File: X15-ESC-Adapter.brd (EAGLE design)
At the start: 101.6 x 41.1 mm, 10 parts, among them J1 IPBT-103-H1-T-S, J2 IPBT-103-H1-T-S, J3 IPBT-103-H1-T-S, J4 IPBT-103-H1-T-S

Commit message: Parts Replaced with New Versions
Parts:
- BACKPLANE_CONNECTIONS: value BACKPLANE_ESC_ADAPTER_PWRBKP -> IPS1-112-01-L-DBKP; device X15-ESC-Adapter:BACKPLANE_ESC_ADAPTER_BKP_PWR -> X15-ESC-Adapter:IPS1-BACKPLANE-PWR
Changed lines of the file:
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@@
 </autorouter>
 <elements>
-<element name="BACKPLANE_CONNECTIONS" library="X15-ESC-Adapter" package="BACKPLANE_ESC_ADAPTER_BKP_PWR" value="BACKPLANE_ESC_ADAPTER_PWRBKP" x="0" y="0" smashed="yes">
+<element name="BACKPLANE_CONNECTIONS" library="X15-ESC-Adapter" library_urn="urn:adsk.eagle:library:38003364" package="IPS1-BACKPLANE-PWR" package3d_urn="urn:adsk.eagle:package:37886186/4" value="IPS1-112-01-L-DBKP" x="0" y="0" smashed="yes">
 <attribute name="NAME" x="36.83" y="32.639" size="1.27" layer="25"/>
 </element>
-<element name="H1" library="X15-ESC-Adapter" package="6-32-HOLE" package3d_urn="urn:adsk.eagle:package:24384748/2" value="6-32-HOLE" x="3.302" y="37.8968" smashed="yes">
+<element name="H1" library="X15-ESC-Adapter" package="6-32-HOLE" package3d_urn="urn:adsk.eagle:package:37886189/1" value="6-32-HOLE" x="3.302" y="37.8968" smashed="yes">
 <attribute name="NAME" x="3.302" y="40.1828" size="0.6096" layer="25" font="vector" ratio="20" align="bottom-center"/>
 </element>
-<element name="H2" library="X15-ESC-Adapter" package="6-32-HOLE" package3d_urn="urn:adsk.eagle:package:24384748/2" value="6-32-HOLE" x="98.298" y="37.846" smashed="yes">
+<element name="H2" library="X15-ESC-Adapter" package="6-32-HOLE" package3d_urn="urn:adsk.eagle:package:37886189/1" value="6-32-HOLE" x="98.298" y="37.846" smashed="yes">
 <attribute name="NAME" x="98.298" y="40.132" size="0.6096" layer="25" font="vector" ratio="20" align="bottom-center"/>
 <attribute name="VALUE" x="98.298" y="35.56" size="0.6096" layer="27" font="vector" ratio="20" align="top-center"/>
 </element>
-<element name="H3" library="X15-ESC-Adapter" package="6-32-HOLE" package3d_urn="urn:adsk.eagle:package:24384748/2" value="6-32-HOLE" x="3.302" y="17.272" smashed="yes">
+<element name="H3" library="X15-ESC-Adapter" package="6-32-HOLE" package3d_urn="urn:adsk.eagle:package:37886189/1" value="6-32-HOLE" x="3.302" y="17.272" smashed="yes">
 <attribute name="NAME" x="3.302" y="19.558" size="0.6096" layer="25" font="vector" ratio="20" align="bottom-center"/>
 <attribute name="VALUE" x="3.302" y="14.986" size="0.6096" layer="27" font="vector" ratio="20" align="top-center"/>
 </element>
-<element name="H4" library="X15-ESC-Adapter" package="6-32-HOLE" package3d_urn="urn:adsk.eagle:package:24384748/2" value="6-32-HOLE" x="98.298" y="17.272" smashed="yes">
+<element name="H4" library="X15-ESC-Adapter" package="6-32-HOLE" package3d_urn="urn:adsk.eagle:package:37886189/1" value="6-32-HOLE" x="98.298" y="17.272" smashed="yes">
 <attribute name="NAME" x="98.298" y="19.558" size="0.6096" layer="25" font="vector" ratio="20" align="bottom-center"/>
 <attribute name="VALUE" x="98.298" y="14.986" size="0.6096" layer="27" font="vector" ratio="20" align="top-center"/>
 </element>
-<element name="J1" library="X15-ESC-Adapter" package="IPBT-103-H1-T-S" value="IPBT-103-H1-T-S" x="13.9192" y="27.6098" smashed="yes" rot="R90"/>
-<element name="J2" library="X15-ESC-Adapter" package="IPBT-103-H1-T-S" value="IPBT-103-H1-T-S" x="13.97" y="6.985" smashed="yes" rot="R90"/>
-<element name="J3" library="X15-ESC-Adapter" package="IPBT-103-H1-T-S" value="IPBT-103-H1-T-S" x="87.63" y="27.6352" smashed="yes" rot="R270"/>
-<element name="J4" library="X15-ESC-Adapter" package="IPBT-103-H1-T-S" value="IPBT-103-H1-T-S" x="87.6554" y="6.985" smashed="yes" rot="R270"/>
-<element name="LUMENIER_ESC" library="X15-ESC-Adapter" package="LUMENIER" package3d_urn="urn:adsk.eagle:package:24294694/3" value="LUMENIER" x="27.813" y="0.508" smashed="yes"/>
+<element name="J1" library="X15-ESC-Adapter" package="IPBT-103-H1-T-S" package3d_urn="urn:adsk.eagle:package:37886187/2" value="IPBT-103-H1-T-S" x="13.9192" y="27.6098" smashed="yes" rot="R90"/>
+<element name="J2" library="X15-ESC-Adapter" package="IPBT-103-H1-T-S" package3d_urn="urn:adsk.eagle:package:37886187/2" value="IPBT-103-H1-T-S" x="13.97" y="6.985" smashed="yes" rot="R90"/>
+<element name="J3" library="X15-ESC-Adapter" package="IPBT-103-H1-T-S" package3d_urn="urn:adsk.eagle:package:37886187/2" value="IPBT-103-H1-T-S" x="87.63" y="27.6352" smashed="yes" rot="R270"/>
+<element name="J4" library="X15-ESC-Adapter" package="IPBT-103-H1-T-S" package3d_urn="urn:adsk.eagle:package:37886187/2" value="IPBT-103-H1-T-S" x="87.6554" y="6.985" smashed="yes" rot="R270"/>
+<element name="LUMENIER_ESC" library="X15-ESC-Adapter" package="LUMENIER" package3d_urn="urn:adsk.eagle:package:37886188/1" value="LUMENIER" x="27.813" y="0.508" smashed="yes"/>
 </elements>
 <signals>
@@
 <via x="56.1086" y="28.448" extent="1-16" drill="0.35"/>
 <via x="53.1622" y="28.3718" extent="1-16" drill="0.35"/>
+<wire x1="65.024" y1="36.322" x2="65.024" y2="38.862" width="0" layer="19" extent="1-1"/>
+<wire x1="62.484" y1="38.862" x2="65.024" y2="38.862" width="0" layer="19" extent="1-1"/>
+<wire x1="62.484" y1="36.322" x2="65.024" y2="36.322" width="0" layer="19" extent="1-1"/>
+<wire x1="59.944" y1="38.862" x2="62.484" y2="38.862" width="0" layer="19" extent="1-1"/>
+<wire x1="59.944" y1="36.322" x2="62.484" y2="36.322" width="0" layer="19" extent="1-1"/>
+<wire x1="57.404" y1="38.862" x2="59.944" y2="38.862" width="0" layer="19" extent="1-1"/>
+<wire x1="57.404" y1="36.322" x2="59.944" y2="36.322" width="0" layer="19" extent="1-1"/>
+<wire x1="56.4642" y1="34.036" x2="57.404" y2="36.322" width="0" layer="19" extent="1-1"/>
+<wire x1="56.9722" y1="33.0962" x2="56.4642" y2="34.036" width="0" layer="19" extent="1-1"/>
+<wire x1="54.864" y1="38.862" x2="57.404" y2="38.862" width="0" layer="19" extent="1-1"/>
+<wire x1="54.864" y1="36.322" x2="57.404" y2="36.322" width="0" layer="19" extent="1-1"/>
+<wire x1="52.324" y1="38.862" x2="54.864" y2="38.862" width="0" layer="19" extent="1-1"/>
+<wire x1="52.324" y1="36.322" x2="54.864" y2="36.322" width="0" layer="19" extent="1-1"/>
+<wire x1="52.197" y1="34.2392" x2="52.324" y2="36.322" width="0" layer="19" extent="1-1"/>
+<wire x1="53.8226" y1="32.9946" x2="52.197" y2="34.2392" width="0" layer="19" extent="1-1"/>
+<wire x1="55.303" y1="30.878" x2="53.8226" y2="32.9946" width="0" layer="19" extent="1-1"/>
+<wire x1="56.1086" y1="28.448" x2="55.303" y2="30.878" width="0" layer="19" extent="1-1"/>
+<wire x1="53.1622" y1="28.3718" x2="56.1086" y2="28.448" width="0" layer="19" extent="1-1"/>
+<wire x1="59.0296" y1="29.21" x2="56.1086" y2="28.448" width="0" layer="19" extent="1-1"/>
+<wire x1="58.9534" y1="27.432" x2="59.0296" y2="29.21" width="0" layer="19" extent="1-1"/>
 </signal>
 <signal name="GND">
@@
 <via x="46.3042" y="33.274" extent="1-16" drill="0.35"/>
 <via x="48.641" y="33.782" extent="1-16" drill="0.35"/>
+<wire x1="49.784" y1="36.322" x2="49.784" y2="38.862" width="0" layer="19" extent="1-1"/>
+<wire x1="47.244" y1="38.862" x2="49.784" y2="38.862" width="0" layer="19" extent="1-1"/>
+<wire x1="47.244" y1="36.322" x2="49.784" y2="36.322" width="0" layer="19" extent="1-1"/>
+<wire x1="44.704" y1="38.862" x2="47.244" y2="38.862" width="0" layer="19" extent="1-1"/>
+<wire x1="44.704" y1="36.322" x2="47.244" y2="36.322" width="0" layer="19" extent="1-1"/>
+<wire x1="43.815" y1="34.29" x2="44.704" y2="36.322" width="0" layer="19" extent="1-1"/>
+<wire x1="42.164" y1="38.862" x2="44.704" y2="38.862" width="0" layer="19" extent="1-1"/>
+<wire x1="42.164" y1="36.322" x2="44.704" y2="36.322" width="0" layer="19" extent="1-1"/>
+<wire x1="39.624" y1="38.862" x2="42.164" y2="38.862" width="0" layer="19" extent="1-1"/>
+<wire x1="39.624" y1="36.322" x2="42.164" y2="36.322" width="0" layer="19" extent="1-1"/>
+<wire x1="37.084" y1="38.862" x2="39.624" y2="38.862" width="0" layer="19" extent="1-1"/>
+<wire x1="37.084" y1="36.322" x2="39.624" y2="36.322" width="0" layer="19" extent="1-1"/>
+<wire x1="46.3042" y1="33.274" x2="43.815" y2="34.29" width="0" layer="19" extent="1-1"/>
+<wire x1="48.641" y1="33.782" x2="46.3042" y2="33.274" width="0" layer="19" extent="1-1"/>
+<wire x1="46.323" y1="30.878" x2="46.3042" y2="33.274" width="0" layer="19" extent="1-1"/>
+<wire x1="46.0502" y1="28.702" x2="46.323" y2="30.878" width="0" layer="19" extent="1-1"/>
+<wire x1="42.3418" y1="31.75" x2="43.815" y2="34.29" width="0" layer="19" extent="1-1"/>
+<wire x1="40.9194" y1="31.877" x2="42.3418" y2="31.75" width="0" layer="19" extent="1-1"/>
+<wire x1="40.5892" y1="29.6164" x2="40.9194" y2="31.877" width="0" layer="19" extent="1-1"/>
+<wire x1="42.8498" y1="29.464" x2="40.5892" y2="29.6164" width="0" layer="19" extent="1-1"/>
 </signal>
 </signals>
@@
 </drawing>
 <compatibility>
+<note version="8.2" severity="warning">
+Since Version 8.2, EAGLE supports online libraries. The ids
+of those online libraries will not be understood (or retained)
+with this version.
+</note>
 <note version="8.3" severity="warning">
 Since Version 8.3, EAGLE supports URNs for individual library

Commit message: Fixed strange things
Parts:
- BACKPLANE_CONNECTIONS: value IPS1-112-01-L-DBKP -> IPS1-112-01-L-D; device X15-ESC-Adapter:IPS1-BACKPLANE-PWR -> X15-ESC-Adapter:IPS1-BACKPLANE_ESC_ADAPTER_ESC_PWR

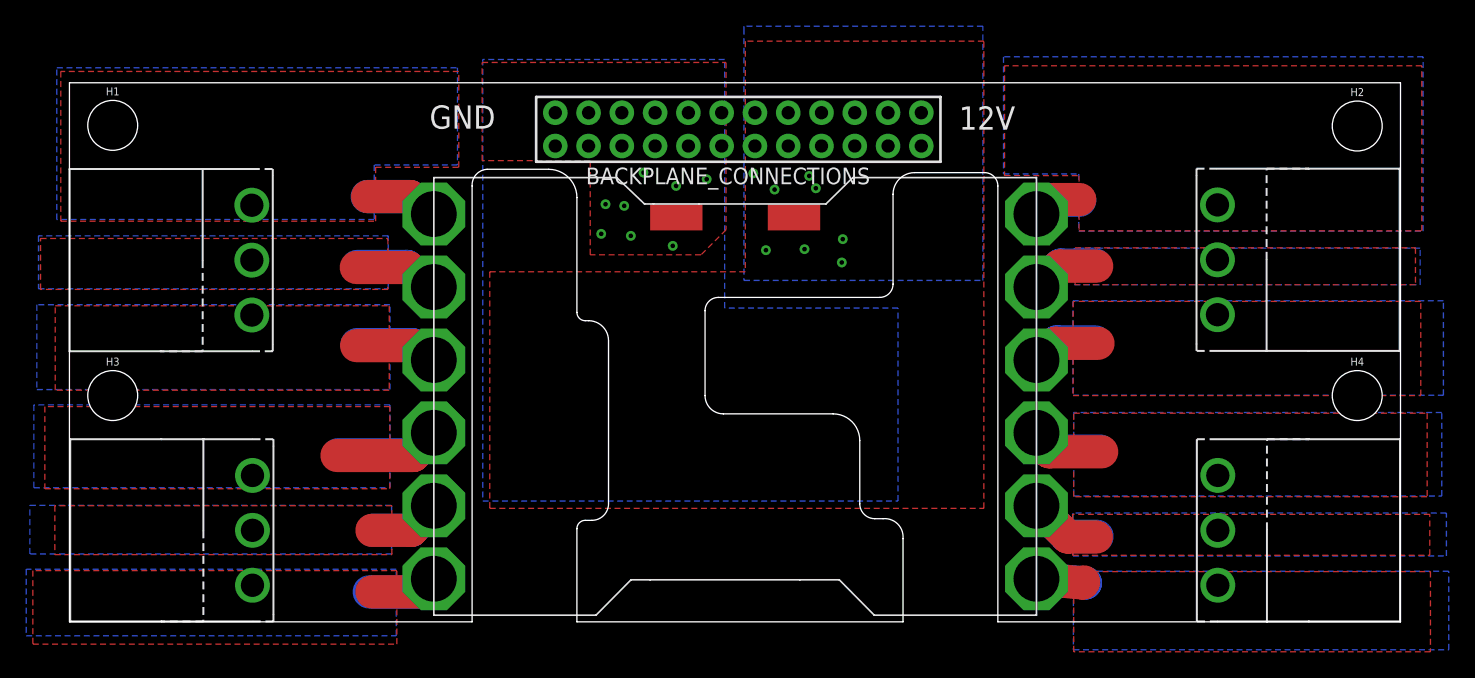
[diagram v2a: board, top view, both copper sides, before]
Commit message: Adjusted thermals
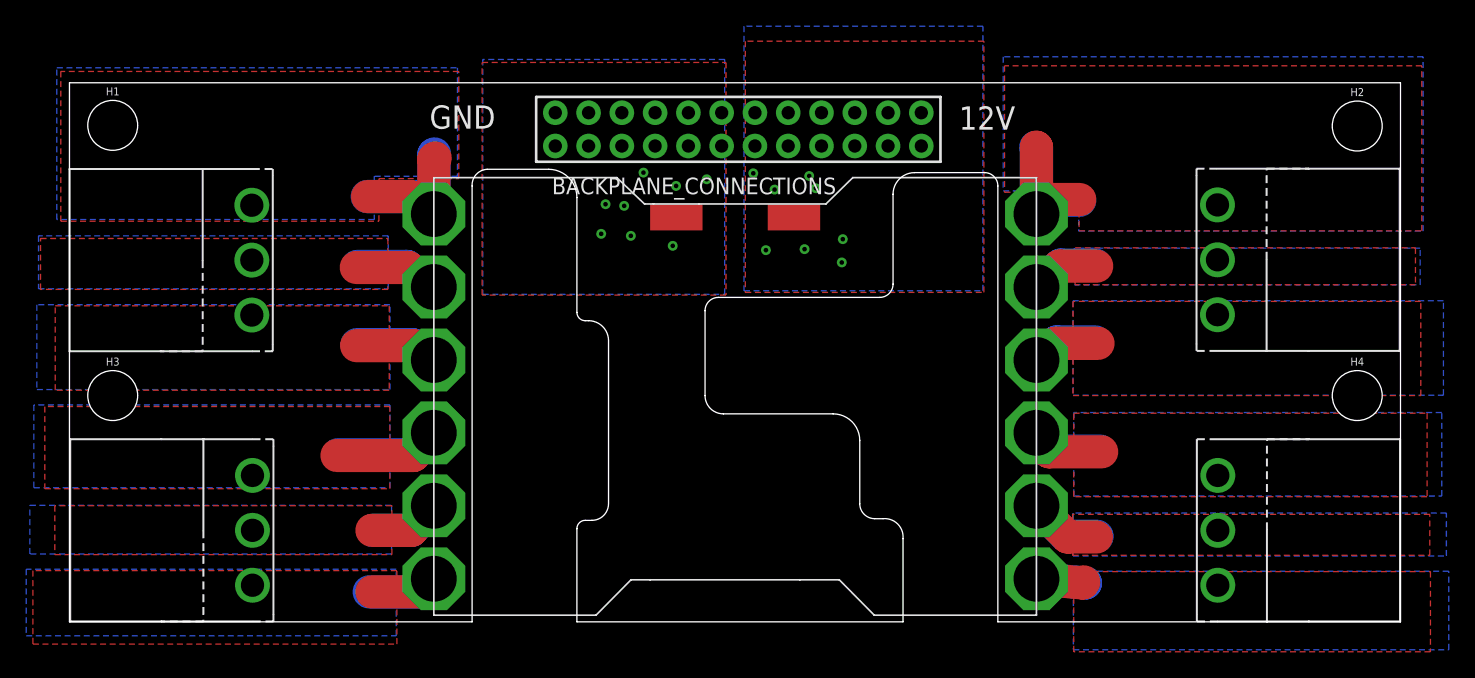
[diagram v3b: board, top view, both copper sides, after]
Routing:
- net ESC3_B: track 7.41 -> 17.6 mm
- net ESC1_B: track 11.0 -> 20.1 mm
